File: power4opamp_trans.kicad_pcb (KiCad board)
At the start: 2 copper layers, 49.5 x 35 mm, 16 parts, among them J1 Conn_01x03, J2 Conn_01x03, U1 L78L12, U2 L79L12

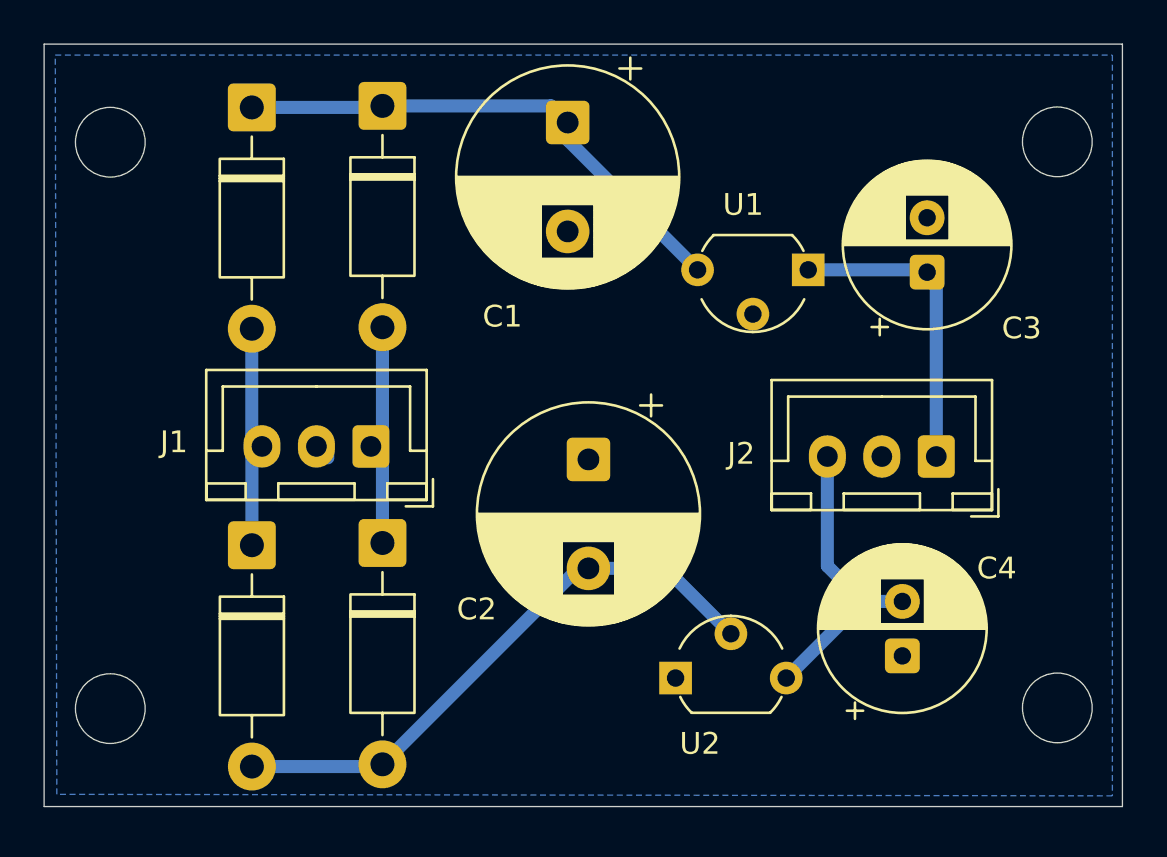
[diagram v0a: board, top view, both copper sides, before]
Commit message: 耐圧を35Vに変更して配置を修正
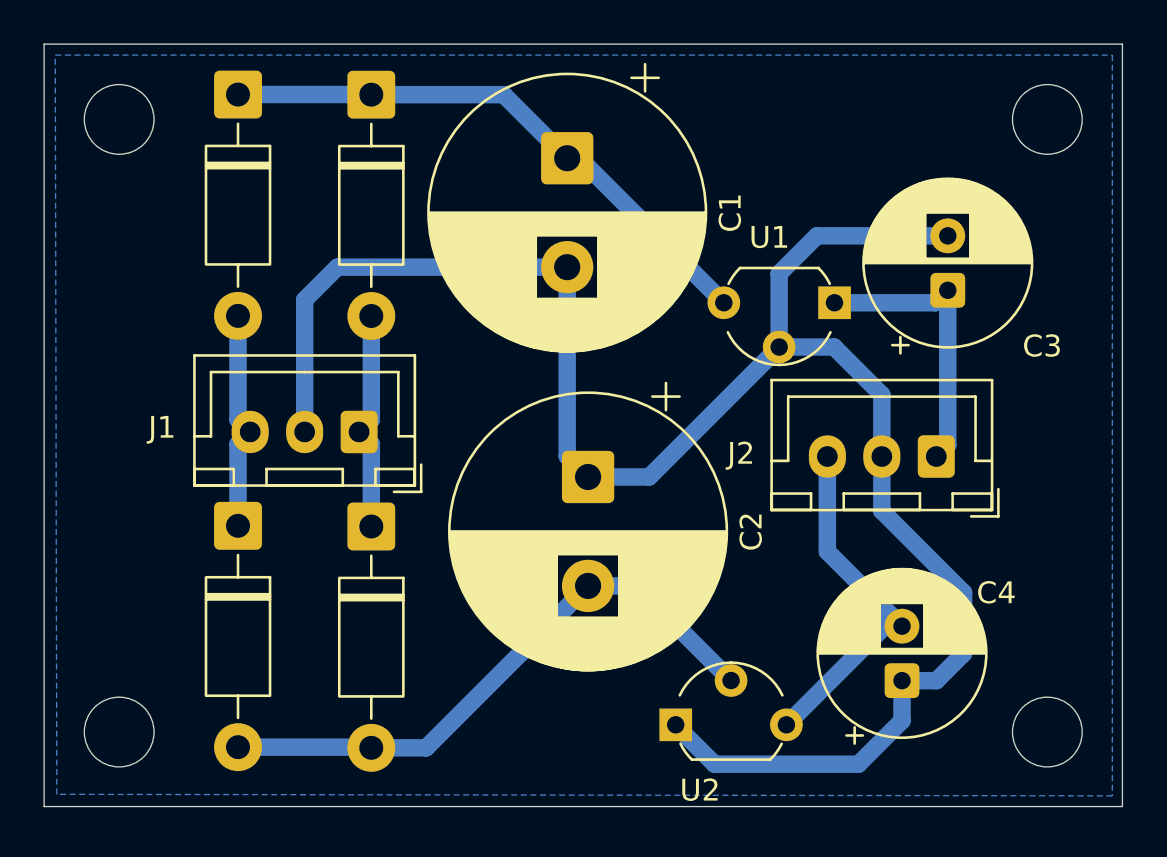
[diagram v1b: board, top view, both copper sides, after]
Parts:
- C1, C2: value 25V1000uF -> 35V1000uF; footprint Capacitor_THT:CP_Radial_D10.0mm_P5.00mm -> Capacitor_THT:CP_Radial_D12.5mm_P5.00mm
- D1, D2, D3, D4: value 1N5817 -> 30V1A
- U1: value L78L12 -> L78L15
- U2: value L79L12 -> L79L15
- moved U2 2.15 mm to (77.0, 96.5)
- moved U1 1.93 mm to (84.2, 77.6)
- moved C1 1.64 mm to (72.0, 70.7)
- moved C3 1.26 mm to (89.4, 76.8)
- moved H4 1.20 mm to (94.0, 97.1)
- moved H3 1.15 mm to (51.4, 97.1)
- moved C4 1.14 mm to (87.3, 94.7)
- moved H2 1.13 mm to (94.0, 69.0)
- moved H1 1.12 mm to (51.4, 69.0)
- moved D3 1.09 mm to (56.9, 87.6)
- moved D1 0.91 mm to (63.0, 87.6)
- moved D4 0.87 mm to (56.9, 67.8)
- moved J1 0.86 mm to (62.4, 83.3)
- moved C2 0.81 mm to (72.9, 85.4)
- moved D2 0.73 mm to (63.0, 67.8)
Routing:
- net GNDPWR: track 0.53 -> 88.0 mm
- net Net-(D2-K): track 24.2 -> 27.2 mm
- net Net-(J2-Pin_1): track 15.1 -> 13.3 mm
- net Net-(J2-Pin_3): track 14.6 -> 16.4 mm
- net Net-(D1-K): track 11.1 -> 10.1 mm
- net Net-(D1-A): track 28.0 -> 28.8 mm
